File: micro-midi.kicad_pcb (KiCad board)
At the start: 2 copper layers, 33.5 x 25 mm, 14 parts, among them J1 AudioJack3, J2 Conn_01x04_Male, J3 AudioJack3, U1 74HC04, U2 6N137

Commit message: put revision on silkscreen
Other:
- board text added: "micro midi rev 0.3.0"
- board text removed: "micro midi"
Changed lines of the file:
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@@
     (effects (font (size 1 1) (thickness 0.15)) (justify left mirror))
   )
-  (gr_text "micro midi" (at 102.108 42.164) (layer B.SilkS)
+  (gr_text "micro midi rev 0.3.0" (at 102.108 42.164) (layer B.SilkS)
     (effects (font (size 1 1) (thickness 0.15)) (justify left mirror))
   )

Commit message: add ferrites to board
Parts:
- added FB1: 600R @ 100Mhz, Resistor_SMD:R_0805_2012Metric_Pad1.15x1.40mm_HandSolder, F.Cu at (86.7, 34.5)
- added FB2: 600R @ 100Mhz, Resistor_SMD:R_0805_2012Metric_Pad1.15x1.40mm_HandSolder, F.Cu at (86.7, 37.5)
- added FB3: 600R @ 100Mhz, Resistor_SMD:R_0805_2012Metric_Pad1.15x1.40mm_HandSolder, F.Cu at (91.5, 34.5)
- added FB4: 600R @ 100Mhz, Resistor_SMD:R_0805_2012Metric_Pad1.15x1.40mm_HandSolder, F.Cu at (91.5, 37.5)
- R3, R4: value 470 -> 470R
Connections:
- J1 pad R: Net-(D1-Pad2) -> Net-(FB2-Pad2)
- J1 pad T: Net-(J1-PadT) -> Net-(FB1-Pad2)
- J3 pad R: Net-(J3-PadR) -> Net-(FB4-Pad1)
- J3 pad T: Net-(J3-PadT) -> Net-(FB3-Pad1)
- R1 pad 2: Net-(J1-PadT) -> Net-(FB1-Pad1)
- R5 pad 1: Net-(J3-PadT) -> Net-(FB3-Pad2)
- R6 pad 1: Net-(J3-PadR) -> Net-(FB4-Pad2)

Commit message: rough placement for ferrites
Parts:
- moved FB4 26.5 mm to (87.2, 63.6)
- moved FB3 25.5 mm to (87.2, 59.6)
- moved FB1 12.9 mm to (87.2, 47.4), turned to 180 degrees
- moved FB2 3.98 mm to (87.2, 41.4), turned to 180 degrees
- moved R5 1.68 mm to (87.2, 57.6)
- moved R3 1.20 mm to (87.2, 55.6)
- moved R4 0.96 mm to (87.2, 49.4)
- moved D2 0.73 mm to (87.2, 53.6)
- moved R1 0.68 mm to (87.2, 45.4)
- moved D3 0.52 mm to (87.2, 51.4)
- moved J3 0.40 mm to (72.0, 57.6)
- moved R6 0.36 mm to (87.2, 61.6)
- moved D1 0.34 mm to (87.2, 43.4)
- moved J1 0.15 mm to (72.0, 47.4)
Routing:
- net Net-(J3-PadT): track 3.62 -> 0.00 mm
- net Net-(FB3-Pad1): track 0.00 -> 3.62 mm

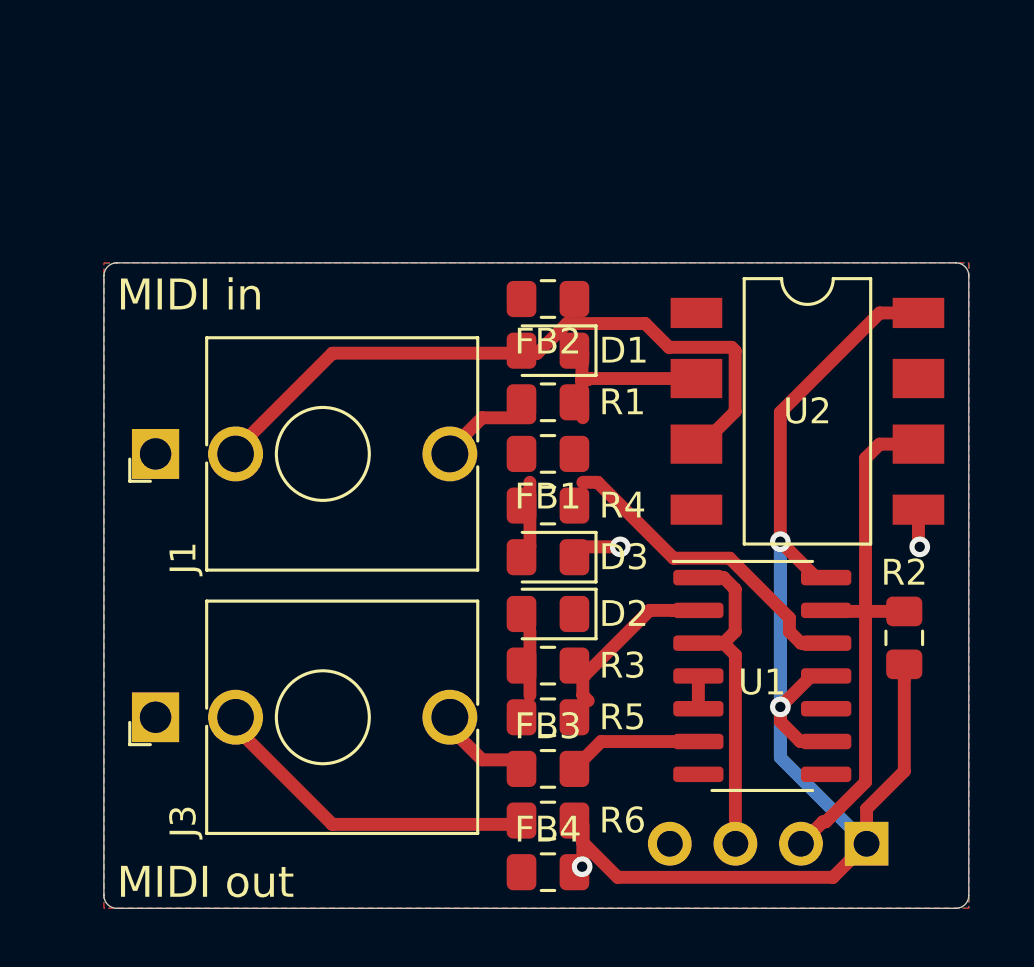
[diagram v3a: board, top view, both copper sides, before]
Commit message: un-cross some tracks
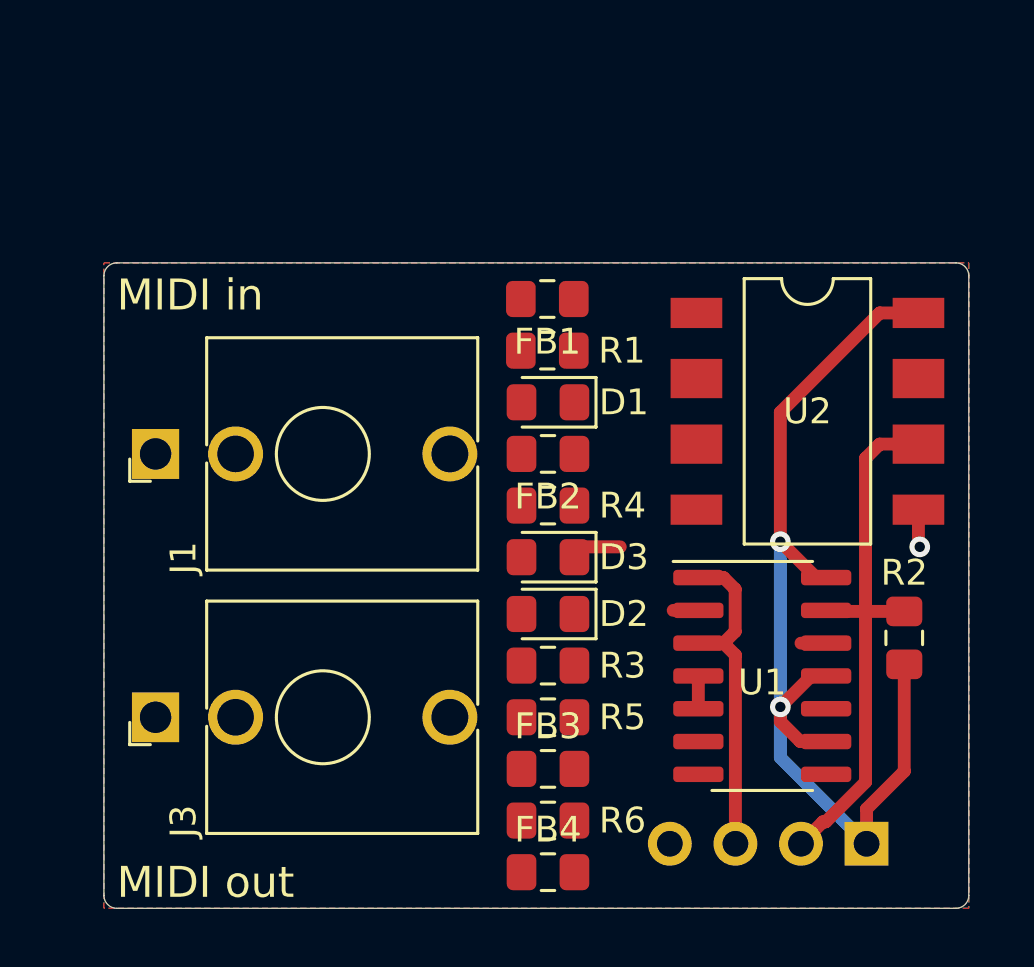
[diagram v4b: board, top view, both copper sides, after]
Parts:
- moved FB1 6.00 mm to (87.2, 41.4)
- moved FB2 6.00 mm to (87.2, 47.4)
- moved R1 2.00 mm to (87.2, 43.4)
- moved D1 2.00 mm to (87.2, 45.4)
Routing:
- net Net-(D1-Pad2): track 26.2 -> 0.24 mm
- net +5V: track 54.3 -> 39.9 mm, vias 3 -> 2
- net Net-(J3-PadR): track 13.0 -> 0.00 mm
- net Net-(R4-Pad2): track 12.3 -> 0.97 mm
- net Net-(D1-Pad1): track 6.96 -> 0.00 mm
- net Net-(R3-Pad2): track 6.54 -> 0.98 mm
- net Net-(R5-Pad2): track 4.77 -> 0.00 mm
- net Net-(J1-PadT): track 3.62 -> 0.00 mm
- net Net-(FB3-Pad1): track 3.62 -> 0.00 mm
- net Net-(D3-Pad2): track 2.50 -> 0.00 mm
- net Net-(D2-Pad2): track 2.50 -> 0.00 mm
- net GND: vias 2 -> 1

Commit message: fix board size
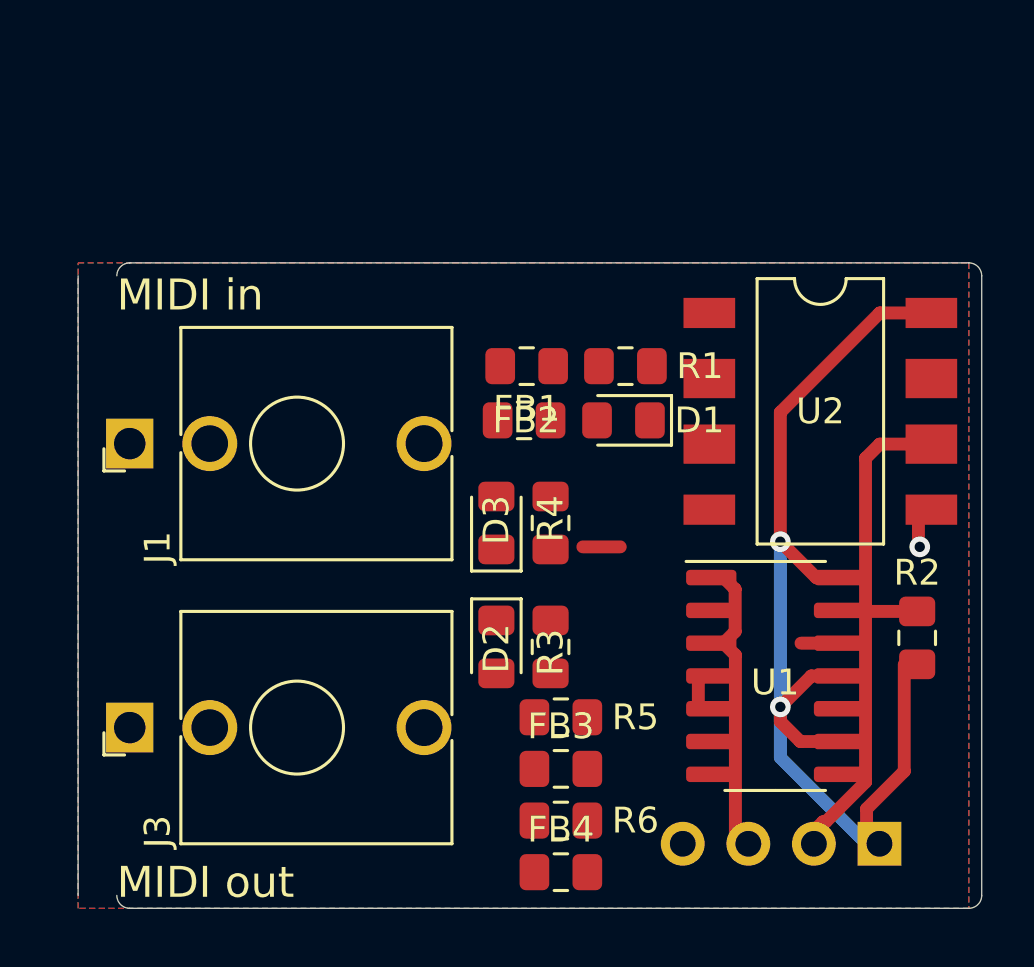
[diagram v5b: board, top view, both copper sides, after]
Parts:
- moved R1 3.08 mm to (90.2, 44.0)
- moved D1 3.01 mm to (90.1, 46.1)
- moved FB1 2.72 mm to (86.4, 44.0)
- moved D3 2.40 mm to (85.2, 50.1), turned to 90 degrees
- moved D2 2.37 mm to (85.2, 54.9), turned to 270 degrees
- moved FB2 1.60 mm to (86.3, 46.1)
- moved J1 1.08 mm to (71.0, 47.0)
- moved J3 1.08 mm to (71.0, 58.0)
- moved R3 0.73 mm to (87.3, 54.9), turned to 90 degrees
- moved R4 0.68 mm to (87.3, 50.1), turned to 270 degrees
- moved FB3 0.50 mm to (87.7, 59.6)
- moved FB4 0.50 mm to (87.7, 63.6)
- moved J2 0.50 mm to (100.0, 62.5)
- moved R2 0.50 mm to (101.5, 54.5)
- moved R5 0.50 mm to (87.7, 57.6)
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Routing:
- net Net-(R3-Pad2): track 0.98 -> 0.00 mm
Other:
- board size 33.5 x 25 mm -> 35 x 25 mm

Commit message: increase board size some more
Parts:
- moved J1 1.10 mm to (69.9, 47.0)
- moved J3 1.10 mm to (69.9, 58.0)
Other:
- board size 35 x 25 mm -> 36 x 25 mm
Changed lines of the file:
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@@
     (add_net "Net-(FB4-Pad1)")
     (add_net "Net-(FB4-Pad2)")
-    (add_net "Net-(J1-PadS)")
     (add_net "Net-(J2-Pad2)")
     (add_net "Net-(J2-Pad3)")
@@
     (add_net "Net-(R4-Pad2)")
     (add_net "Net-(R5-Pad2)")
-    (add_net "Net-(U1-Pad10)")
     (add_net "Net-(U1-Pad4)")
-    (add_net "Net-(U1-Pad8)")
-    (add_net "Net-(U2-Pad1)")
-    (add_net "Net-(U2-Pad7)")
   )
   (module Resistor_SMD:R_0805_2012Metric_Pad1.15x1.40mm_HandSolder (layer F.Cu)
@@
   )
   (module Connector_Audio:Jack_3.5mm_QingPu_WQP-PJ398SM_Vertical_CircularHoles (layer F.Cu)
-    (at 71 58 90)
+    (at 69.9 58 90)
     (descr "TRS 3.5mm, vertical, Thonkiconn, PCB mount, (http://www.qingpu-electronics.com/en/products/WQP-PJ398SM-362.html)")
     (tags "WQP-PJ398SM WQP-PJ301M-12 TRS 3.5mm mono vertical jack thonkiconn qingpu")
@@
   )
   (module Connector_Audio:Jack_3.5mm_QingPu_WQP-PJ398SM_Vertical_CircularHoles (layer F.Cu)
-    (at 71 47 90)
+    (at 69.9 47 90)
     (descr "TRS 3.5mm, vertical, Thonkiconn, PCB mount, (http://www.qingpu-electronics.com/en/products/WQP-PJ398SM-362.html)")
     (tags "WQP-PJ398SM WQP-PJ301M-12 TRS 3.5mm mono vertical jack thonkiconn qingpu")
@@
   )
   (gr_arc (start 103.5 64.5) (end 103.5 65) (angle -90) (layer Edge.Cuts) (width 0.05))
-  (gr_arc (start 71 64.5) (end 70.5 64.5) (angle -90) (layer Edge.Cuts) (width 0.05))
-  (gr_arc (start 71 40.5) (end 71 40) (angle -90) (layer Edge.Cuts) (width 0.05))
+  (gr_arc (start 68.5 64.5) (end 68 64.5) (angle -90) (layer Edge.Cuts) (width 0.05))
+  (gr_arc (start 68.5 40.5) (end 68.5 40) (angle -90) (layer Edge.Cuts) (width 0.05))
   (gr_arc (start 103.5 40.5) (end 104 40.5) (angle -90) (layer Edge.Cuts) (width 0.05))
-  (gr_line (start 69 40.5) (end 69 64.5) (layer Edge.Cuts) (width 0.05))
+  (gr_line (start 68 40.5) (end 68 64.5) (layer Edge.Cuts) (width 0.05))
   (gr_line (start 104 40.5) (end 104 64.5) (layer Edge.Cuts) (width 0.05))
-  (gr_line (start 71 40) (end 103.5 40) (layer Edge.Cuts) (width 0.05))
-  (gr_line (start 71 65) (end 103.5 65) (layer Edge.Cuts) (width 0.05))
-  (gr_text "MIDI out" (at 70.5 64) (layer F.SilkS)
+  (gr_line (start 68.5 40) (end 103.5 40) (layer Edge.Cuts) (width 0.05))
+  (gr_line (start 68.5 65) (end 103.5 65) (layer Edge.Cuts) (width 0.05))
+  (gr_text "MIDI out" (at 68.2 63.9) (layer F.SilkS)
     (effects (font (size 1.2 1.2) (thickness 0.3)) (justify left))
   )
-  (gr_text "MIDI in" (at 70.5 41.25) (layer F.SilkS)
+  (gr_text "MIDI in" (at 68.2 41.2) (layer F.SilkS)
     (effects (font (size 1.2 1.2) (thickness 0.3)) (justify left))
   )

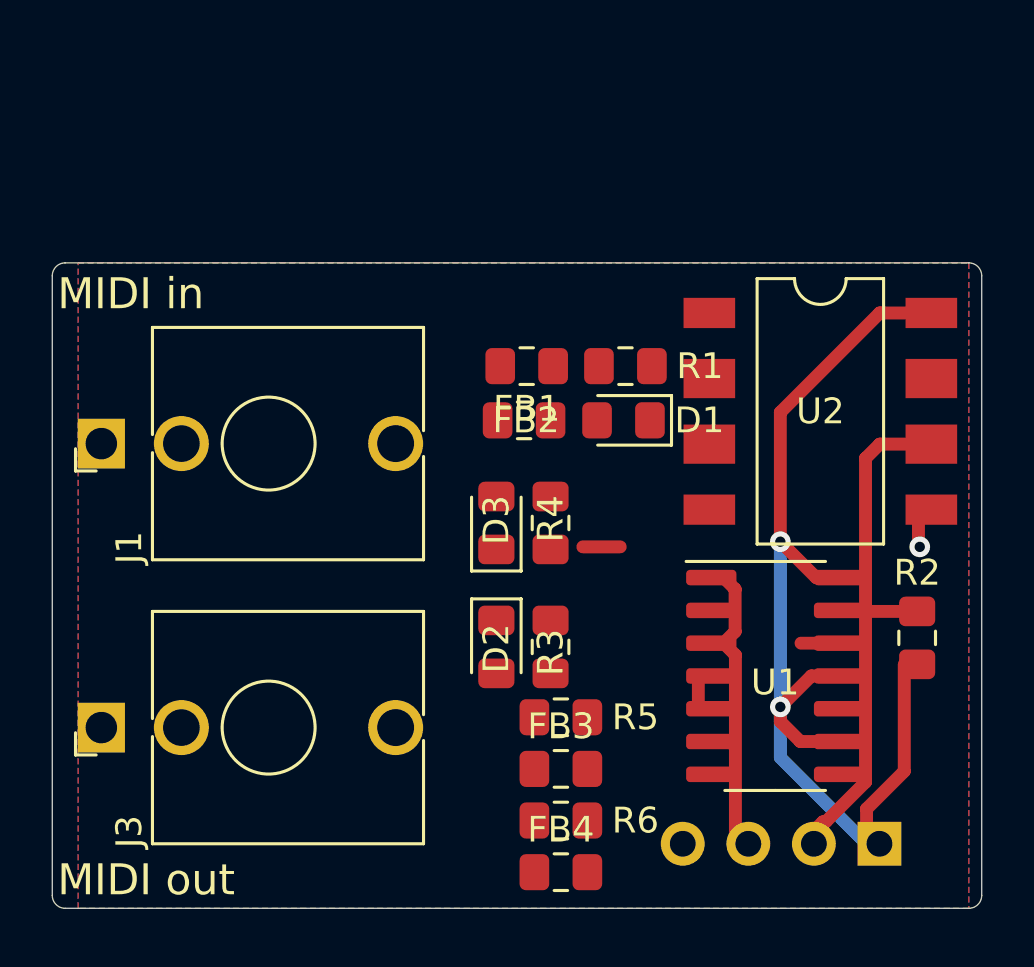
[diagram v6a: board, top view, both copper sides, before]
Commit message: delete tracks, clean up placement and copper fills
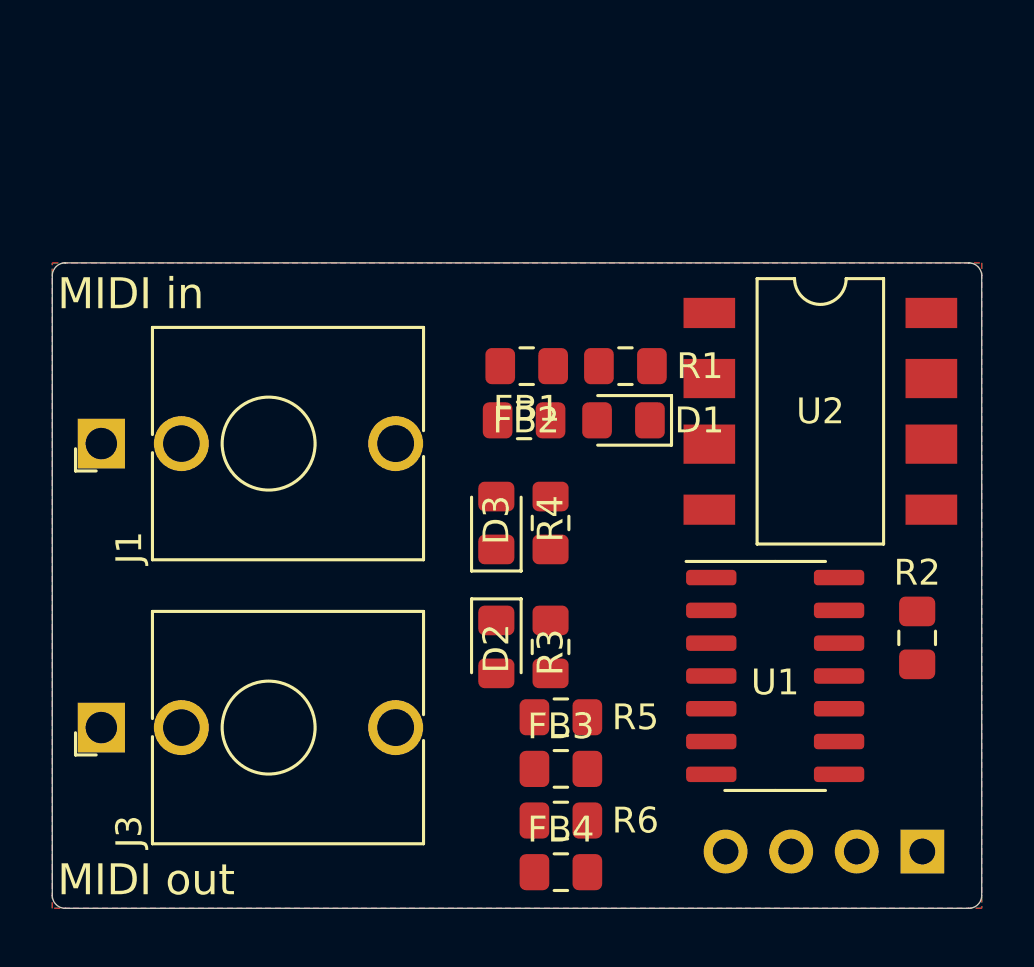
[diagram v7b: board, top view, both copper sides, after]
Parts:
- moved J2 1.69 mm to (101.7, 62.8)
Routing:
- net +5V: track 39.9 -> 0.00 mm, vias 2 -> 0
- net Net-(J2-Pad2): track 21.3 -> 0.00 mm
- net Net-(J2-Pad3): track 12.8 -> 0.00 mm
- net GND: track 2.91 -> 0.00 mm, vias 1 -> 0
- net Net-(U1-Pad4): track 1.27 -> 0.00 mm
- net Net-(R4-Pad2): track 0.97 -> 0.00 mm
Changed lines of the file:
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@@
     (thickness 1.6)
     (drawings 16)
-    (tracks 42)
+    (tracks 0)
     (zones 0)
     (modules 18)
@@
   )
   (layers
-    (0 F.Cu signal hide)
+    (0 F.Cu signal)
     (31 B.Cu signal hide)
     (32 B.Adhes user)
@@
     (user_trace_width 0.5)
     (trace_clearance 0.2)
-    (zone_clearance 0.1)
+    (zone_clearance 0.254)
     (zone_45_only no)
     (trace_min 0.2)
@@
   )
   (module Connector_PinHeader_2.54mm:PinHeader_1x04_P2.54mm_Vertical (layer B.Cu)
-    (at 100.04 62.5 90)
+    (at 101.7 62.8 90)
     (descr "Through hole straight pin header, 1x04, 2.54mm pitch, single row")
     (tags "Through hole pin header THT 1x04 2.54mm single row")
@@
     (effects (font (size 1.2 1.2) (thickness 0.3)) (justify left))
   )
-  (segment (start 93.19 47.02) (end 92.95 47.02) (width 0.5) (layer F.Cu) (net 1) (status 30))
-  (segment (start 101 59.69) (end 101 55.55) (width 0.5) (layer F.Cu) (net 3) (status 20))
-  (segment (start 99.54 61.15) (end 101 59.69) (width 0.5) (layer F.Cu) (net 3))
-  (segment (start 99.54 62.5) (end 99.54 61.15) (width 0.5) (layer F.Cu) (net 3) (status 10))
-  (via (at 96.2 57.2) (size 0.8) (drill 0.4) (layers F.Cu B.Cu) (net 3))
-  (segment (start 96.2 59.16) (end 99.54 62.5) (width 0.5) (layer B.Cu) (net 3) (status 20))
-  (segment (start 96.2 57.2) (end 96.2 59.16) (width 0.5) (layer B.Cu) (net 3))
-  (segment (start 97.4 56) (end 96.2 57.2) (width 0.5) (layer F.Cu) (net 3) (status 10))
-  (segment (start 97.975 56) (end 97.4 56) (width 0.5) (layer F.Cu) (net 3) (status 30))
-  (segment (start 96.2 57.765685) (end 96.2 57.2) (width 0.5) (layer F.Cu) (net 3))
-  (segment (start 96.974315 58.54) (end 96.2 57.765685) (width 0.5) (layer F.Cu) (net 3))
-  (segment (start 97.975 58.54) (end 96.974315 58.54) (width 0.5) (layer F.Cu) (net 3) (status 10))
-  (via (at 96.2 50.8) (size 0.8) (drill 0.4) (layers F.Cu B.Cu) (net 3))
-  (segment (start 96.2 57.2) (end 96.2 50.8) (width 0.5) (layer B.Cu) (net 3))
-  (segment (start 100.05 41.94) (end 101.55 41.94) (width 0.5) (layer F.Cu) (net 3) (status 20))
-  (segment (start 96.2 45.79) (end 100.05 41.94) (width 0.5) (layer F.Cu) (net 3))
-  (segment (start 96.2 50.8) (end 96.2 45.79) (width 0.5) (layer F.Cu) (net 3))
-  (segment (start 97.59 52.19) (end 96.2 50.8) (width 0.5) (layer F.Cu) (net 3) (status 10))
-  (segment (start 97.975 52.19) (end 97.59 52.19) (width 0.5) (layer F.Cu) (net 3) (status 30))
-  (segment (start 98.015 53.5) (end 97.975 53.46) (width 0.5) (layer F.Cu) (net 4) (status 30))
-  (segment (start 99.5 60.108544) (end 99.5 53.5) (width 0.5) (layer F.Cu) (net 4))
-  (segment (start 97.849999 61.650001) (end 97.958543 61.650001) (width 0.5) (layer F.Cu) (net 4))
-  (segment (start 97 62.5) (end 97.849999 61.650001) (width 0.5) (layer F.Cu) (net 4) (status 10))
-  (segment (start 101 53.5) (end 99.5 53.5) (width 0.5) (layer F.Cu) (net 4) (status 10))
-  (segment (start 97.958543 61.650001) (end 99.5 60.108544) (width 0.5) (layer F.Cu) (net 4))
-  (segment (start 99.5 53.5) (end 98.015 53.5) (width 0.5) (layer F.Cu) (net 4) (status 20))
-  (segment (start 100.05 47.02) (end 99.5 47.57) (width 0.5) (layer F.Cu) (net 4))
-  (segment (start 99.5 47.57) (end 99.5 53.5) (width 0.5) (layer F.Cu) (net 4))
-  (segment (start 101.55 47.02) (end 100.05 47.02) (width 0.5) (layer F.Cu) (net 4) (status 10))
-  (segment (start 88.55 51) (end 90 51) (width 0.5) (layer F.Cu) (net 5) (status 10))
-  (segment (start 101.55 49.56) (end 101.55 50.95) (width 0.5) (layer F.Cu) (net 5) (status 10))
-  (via (at 101.6 51) (size 0.8) (drill 0.4) (layers F.Cu B.Cu) (net 5))
-  (segment (start 101.55 50.95) (end 101.6 51) (width 0.5) (layer F.Cu) (net 5))
-  (segment (start 94.45001 54.27999) (end 94 54.73) (width 0.5) (layer F.Cu) (net 8))
-  (segment (start 94.45001 52.64001) (end 94.45001 54.27999) (width 0.5) (layer F.Cu) (net 8))
-  (segment (start 94 52.19) (end 94.45001 52.64001) (width 0.5) (layer F.Cu) (net 8))
-  (segment (start 93.025 52.19) (end 94 52.19) (width 0.5) (layer F.Cu) (net 8) (status 10))
-  (segment (start 94 54.73) (end 93.025 54.73) (width 0.5) (layer F.Cu) (net 8) (status 20))
-  (segment (start 94.46 55.19) (end 94 54.73) (width 0.5) (layer F.Cu) (net 8))
-  (segment (start 94.46 62.5) (end 94.46 55.19) (width 0.5) (layer F.Cu) (net 8) (status 10))
-  (segment (start 97 54.73) (end 97.975 54.73) (width 0.5) (layer F.Cu) (net 10) (status 30))
-  (segment (start 93.025 57.27) (end 93.025 56) (width 0.5) (layer F.Cu) (net 12) (status 30))
   (zone (net 5) (net_name GND) (layer F.Cu) (hatch edge 0.508)
-    (connect_pads (clearance 0.1))
-    (min_thickness 0.1)
-    (fill yes (arc_segments 32) (thermal_gap 0.508) (thermal_bridge_width 0.508))
-    (polygon
-      (pts
-        (xy 103.5 65) (xy 69 65) (xy 69 40) (xy 103.5 40)
-      )
-    )
-  )
-  (zone (net 5) (net_name GND) (layer B.Cu) (hatch edge 0.508)
-    (connect_pads (clearance 0.508))
+    (connect_pads (clearance 0.254))
     (min_thickness 0.254)
     (fill yes (arc_segments 32) (thermal_gap 0.508) (thermal_bridge_width 0.508))
     (polygon
       (pts
-        (xy 103.5 65) (xy 69 65) (xy 69 40) (xy 103.5 40)
+        (xy 104 65) (xy 68 65) (xy 68 40) (xy 104 40)
       )
     )
+  )
+  (zone (net 5) (net_name GND) (layer B.Cu) (hatch edge 0.508)
+    (connect_pads (clearance 0.254))
+    (min_thickness 0.254)
+    (fill yes (arc_segments 32) (thermal_gap 0.508) (thermal_bridge_width 0.508))
+    (polygon
+      (pts
+        (xy 104 65) (xy 68 65) (xy 68 40) (xy 104 40)
+      )
+    )

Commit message: precise placement
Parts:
- moved FB4 2.97 mm to (85.2, 62.0)
- moved R5 2.64 mm to (89.3, 59.7)
- moved R4 2.52 mm to (89.6, 51.1), turned to 0 degrees
- moved FB3 2.50 mm to (85.2, 59.7)
- moved R3 2.46 mm to (89.6, 54.0), turned to 0 degrees
- moved R6 1.65 mm to (89.3, 62.0)
- moved FB1 1.54 mm to (85.2, 43.0)
- moved R1 1.35 mm to (89.3, 43.0)
- moved FB2 1.34 mm to (85.2, 45.3)
- moved D1 1.15 mm to (89.3, 45.3)
- moved D3 0.91 mm to (84.3, 50.2)
- moved D2 0.90 mm to (84.3, 54.9), turned to 90 degrees
